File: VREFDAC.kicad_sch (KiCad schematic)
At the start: 11 parts, among them U34 AD7841, U44 AD586, U45 AD586

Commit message: Add component values, some more nets
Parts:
- C160, C161, C162, C163, C164, C165: value ? -> 0.047uF
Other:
- moved on the sheet: C162, C163, C165
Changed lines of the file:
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@@
 	)
 	(junction
-		(at 199.39 48.26)
+		(at 195.58 48.26)
 		(diameter 0)
 		(color 0 0 0 0)
@@
 	)
 	(junction
-		(at 162.56 46.99)
+		(at 166.37 46.99)
 		(diameter 0)
 		(color 0 0 0 0)
@@
 	(wire
 		(pts
-			(xy 162.56 46.99) (xy 162.56 50.8)
+			(xy 166.37 46.99) (xy 166.37 50.8)
 		)
 		(stroke
@@
 	(wire
 		(pts
-			(xy 199.39 48.26) (xy 199.39 50.8)
+			(xy 195.58 48.26) (xy 195.58 50.8)
 		)
 		(stroke
@@
 	(wire
 		(pts
-			(xy 199.39 48.26) (xy 186.69 48.26)
-		)
-		(stroke
-			(width 0)
-			(type default)
-		)
-	)
-	(wire
-		(pts
-			(xy 215.9 31.75) (xy 209.55 31.75)
+			(xy 227.33 31.75) (xy 215.9 31.75)
 		)
 		(stroke
@@
 	(wire
 		(pts
+			(xy 195.58 48.26) (xy 205.74 48.26)
+		)
+		(stroke
+			(width 0)
+			(type default)
+		)
+	)
+	(wire
+		(pts
 			(xy 165.1 121.92) (xy 165.1 148.59)
 		)
@@
 	(wire
 		(pts
-			(xy 162.56 45.72) (xy 162.56 46.99)
+			(xy 166.37 45.72) (xy 166.37 46.99)
 		)
 		(stroke
@@
 	(wire
 		(pts
-			(xy 205.74 48.26) (xy 199.39 48.26)
-		)
-		(stroke
-			(width 0)
-			(type default)
-		)
-	)
-	(wire
-		(pts
 			(xy 215.9 26.67) (xy 215.9 31.75)
 		)
@@
 	(wire
 		(pts
-			(xy 209.55 31.75) (xy 209.55 33.02)
+			(xy 227.33 31.75) (xy 227.33 33.02)
 		)
 		(stroke
@@
 	(wire
 		(pts
+			(xy 195.58 48.26) (xy 186.69 48.26)
+		)
+		(stroke
+			(width 0)
+			(type default)
+		)
+	)
+	(wire
+		(pts
 			(xy 93.98 99.06) (xy 124.46 99.06)
 		)
@@
 	(wire
 		(pts
-			(xy 152.4 46.99) (xy 162.56 46.99)
+			(xy 152.4 46.99) (xy 166.37 46.99)
 		)
 		(stroke
@@
 	(symbol
 		(lib_id "power:GND")
-		(at 209.55 38.1 0)
+		(at 227.33 38.1 0)
 		(mirror y)
 		(unit 1)
@@
 		(fields_autoplaced yes)
 		(property "Reference" "#PWR0229"
-			(at 209.55 44.45 0)
+			(at 227.33 44.45 0)
 			(effects
 				(font
@@
 		)
 		(property "Value" "GND"
-			(at 209.55 43.18 0)
+			(at 227.33 43.18 0)
 			(effects
 				(font
@@
 		)
 		(property "Footprint" ""
-			(at 209.55 38.1 0)
+			(at 227.33 38.1 0)
 			(effects
 				(font
@@
 		)
 		(property "Datasheet" ""
-			(at 209.55 38.1 0)
+			(at 227.33 38.1 0)
 			(effects
 				(font
@@
 		)
 		(property "Description" "Power symbol creates a global label with name \"GND\" , ground"
-			(at 209.55 38.1 0)
+			(at 227.33 38.1 0)
 			(effects
 				(font
@@
 			)
 		)
-		(property "Value" "?"
+		(property "Value" "0.047uF"
 			(at 154.94 54.6162 0)
 			(effects
@@
 			)
 		)
-		(property "Value" "?"
+		(property "Value" "0.047uF"
 			(at 148.59 146.0562 0)
 			(effects
@@
 	(symbol
 		(lib_id "power:+12V")
-		(at 162.56 45.72 0)
+		(at 166.37 45.72 0)
 		(unit 1)
 		(exclude_from_sim no)
@@
 		(dnp no)
 		(property "Reference" "#PWR0231"
-			(at 162.56 49.53 0)
+			(at 166.37 49.53 0)
 			(effects
 				(font
@@
 		)
 		(property "Value" "+12V"
-			(at 162.56 40.64 0)
+			(at 166.37 40.64 0)
 			(effects
 				(font
@@
 		)
 		(property "Footprint" ""
-			(at 162.56 45.72 0)
+			(at 166.37 45.72 0)
 			(effects
 				(font
@@
 		)
 		(property "Datasheet" ""
-			(at 162.56 45.72 0)
+			(at 166.37 45.72 0)
 			(effects
 				(font
@@
 		)
 		(property "Description" "Power symbol creates a global label with name \"+12V\""
-			(at 162.56 45.72 0)
+			(at 166.37 45.72 0)
 			(effects
 				(font
@@
 	(symbol
 		(lib_id "power:GND")
-		(at 162.56 55.88 0)
+		(at 166.37 55.88 0)
 		(unit 1)
 		(exclude_from_sim no)
@@
 		(fields_autoplaced yes)
 		(property "Reference" "#PWR0226"
-			(at 162.56 62.23 0)
+			(at 166.37 62.23 0)
 			(effects
 				(font
@@
 		)
 		(property "Value" "GND"
-			(at 162.56 60.96 0)
+			(at 166.37 60.96 0)
 			(effects
 				(font
@@
 		)
 		(property "Footprint" ""
-			(at 162.56 55.88 0)
+			(at 166.37 55.88 0)
 			(effects
 				(font
@@
 		)
 		(property "Datasheet" ""
-			(at 162.56 55.88 0)
+			(at 166.37 55.88 0)
 			(effects
 				(font
@@
 		)
 		(property "Description" "Power symbol creates a global label with name \"GND\" , ground"
-			(at 162.56 55.88 0)
+			(at 166.37 55.88 0)
 			(effects
 				(font
@@
 			)
 		)
-		(property "Value" "?"
+		(property "Value" "0.047uF"
 			(at 218.44 154.9462 0)
 			(effects
@@
 	(symbol
 		(lib_id "Device:C_Small")
-		(at 199.39 53.34 0)
+		(at 195.58 53.34 0)
 		(unit 1)
 		(exclude_from_sim no)
@@
 		(fields_autoplaced yes)
 		(property "Reference" "C163"
-			(at 201.93 52.0762 0)
+			(at 198.12 52.0762 0)
 			(effects
 				(font
@@
 			)
 		)
-		(property "Value" "?"
-			(at 201.93 54.6162 0)
+		(property "Value" "0.047uF"
+			(at 198.12 54.6162 0)
 			(effects
 				(font
@@
 		)
 		(property "Footprint" "hp16717:HP_0805"
-			(at 199.39 53.34 0)
+			(at 195.58 53.34 0)
 			(effects
 				(font
@@
 		)
 		(property "Datasheet" "~"
-			(at 199.39 53.34 0)
+			(at 195.58 53.34 0)
 			(effects
 				(font
@@
 		)
 		(property "Description" "Unpolarized capacitor, small symbol"
-			(at 199.39 53.34 0)
+			(at 195.58 53.34 0)
 			(effects
 				(font
@@
 	(symbol
 		(lib_id "Device:C_Small")
-		(at 162.56 53.34 0)
+		(at 166.37 53.34 0)
 		(unit 1)
 		(exclude_from_sim no)
@@
 		(fields_autoplaced yes)
 		(property "Reference" "C162"
-			(at 165.1 52.0762 0)
+			(at 168.91 52.0762 0)
 			(effects
 				(font
@@
 			)
 		)
-		(property "Value" "?"
-			(at 165.1 54.6162 0)
+		(property "Value" "0.047uF"
+			(at 168.91 54.6162 0)
 			(effects
 				(font
@@
 		)
 		(property "Footprint" "hp16717:HP_0805"
-			(at 162.56 53.34 0)
+			(at 166.37 53.34 0)
 			(effects
 				(font
@@
 		)
 		(property "Datasheet" "~"
-			(at 162.56 53.34 0)
+			(at 166.37 53.34 0)
 			(effects
 				(font
@@
 		)
 		(property "Description" "Unpolarized capacitor, small symbol"
-			(at 162.56 53.34 0)
+			(at 166.37 53.34 0)
 			(effects
 				(font
@@
 	(symbol
 		(lib_id "Device:C_Small")
-		(at 209.55 35.56 0)
+		(at 227.33 35.56 0)
 		(mirror y)
 		(unit 1)
@@
 		(fields_autoplaced yes)
 		(property "Reference" "C165"
-			(at 207.01 34.2962 0)
+			(at 229.87 34.2962 0)
 			(effects
 				(font
 					(size 1.27 1.27)
 				)
-				(justify left)
+				(justify right)
 			)
 		)
-		(property "Value" "?"
-			(at 207.01 36.8362 0)
+		(property "Value" "0.047uF"
+			(at 229.87 36.8362 0)
 			(effects
 				(font
 					(size 1.27 1.27)
 				)
-				(justify left)
+				(justify right)
 			)
 		)
 		(property "Footprint" "hp16717:HP_0805"
-			(at 209.55 35.56 0)
+			(at 227.33 35.56 0)
 			(effects
 				(font
@@
 		)
 		(property "Datasheet" "~"
-			(at 209.55 35.56 0)
+			(at 227.33 35.56 0)
 			(effects
 				(font
@@
 		)
 		(property "Description" "Unpolarized capacitor, small symbol"
-			(at 209.55 35.56 0)
+			(at 227.33 35.56 0)
 			(effects
 				(font
@@
 	(symbol
 		(lib_id "power:GND")
-		(at 199.39 55.88 0)
+		(at 195.58 55.88 0)
 		(unit 1)
 		(exclude_from_sim no)
@@
 		(fields_autoplaced yes)
 		(property "Reference" "#PWR0227"
-			(at 199.39 62.23 0)
+			(at 195.58 62.23 0)
 			(effects
 				(font
@@
 		)
 		(property "Value" "GND"
-			(at 199.39 60.96 0)
+			(at 195.58 60.96 0)
 			(effects
 				(font
@@
 		)
 		(property "Footprint" ""
-			(at 199.39 55.88 0)
+			(at 195.58 55.88 0)
 			(effects
 				(font
@@
 		)
 		(property "Datasheet" ""
-			(at 199.39 55.88 0)
+			(at 195.58 55.88 0)
 			(effects
 				(font
@@
 		)
 		(property "Description" "Power symbol creates a global label with name \"GND\" , ground"
-			(at 199.39 55.88 0)
+			(at 195.58 55.88 0)
 			(effects
 				(font

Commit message: complete outer layers
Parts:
- U34: footprint Package_QFP:Microchip_PQFP-44_10x10mm_P0.8mm -> hp16717:HP_LQFP-44_10x10mm_P0.8mm
- U44, U45: footprint Package_SO:SOIC-8_3.9x4.9mm_P1.27mm -> hp16717:HP_SO-8_3.9x4.9mm_P1.27mm
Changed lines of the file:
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@@
 			)
 		)
-		(property "Footprint" "Package_SO:SOIC-8_3.9x4.9mm_P1.27mm"
+		(property "Footprint" "hp16717:HP_SO-8_3.9x4.9mm_P1.27mm"
 			(at 217.17 46.99 0)
 			(effects
@@
 			)
 		)
-		(property "Footprint" "Package_QFP:Microchip_PQFP-44_10x10mm_P0.8mm"
+		(property "Footprint" "hp16717:HP_LQFP-44_10x10mm_P0.8mm"
 			(at 127 60.96 0)
 			(effects
@@
 			)
 		)
-		(property "Footprint" "Package_SO:SOIC-8_3.9x4.9mm_P1.27mm"
+		(property "Footprint" "hp16717:HP_SO-8_3.9x4.9mm_P1.27mm"
 			(at 214.63 132.08 0)
 			(effects

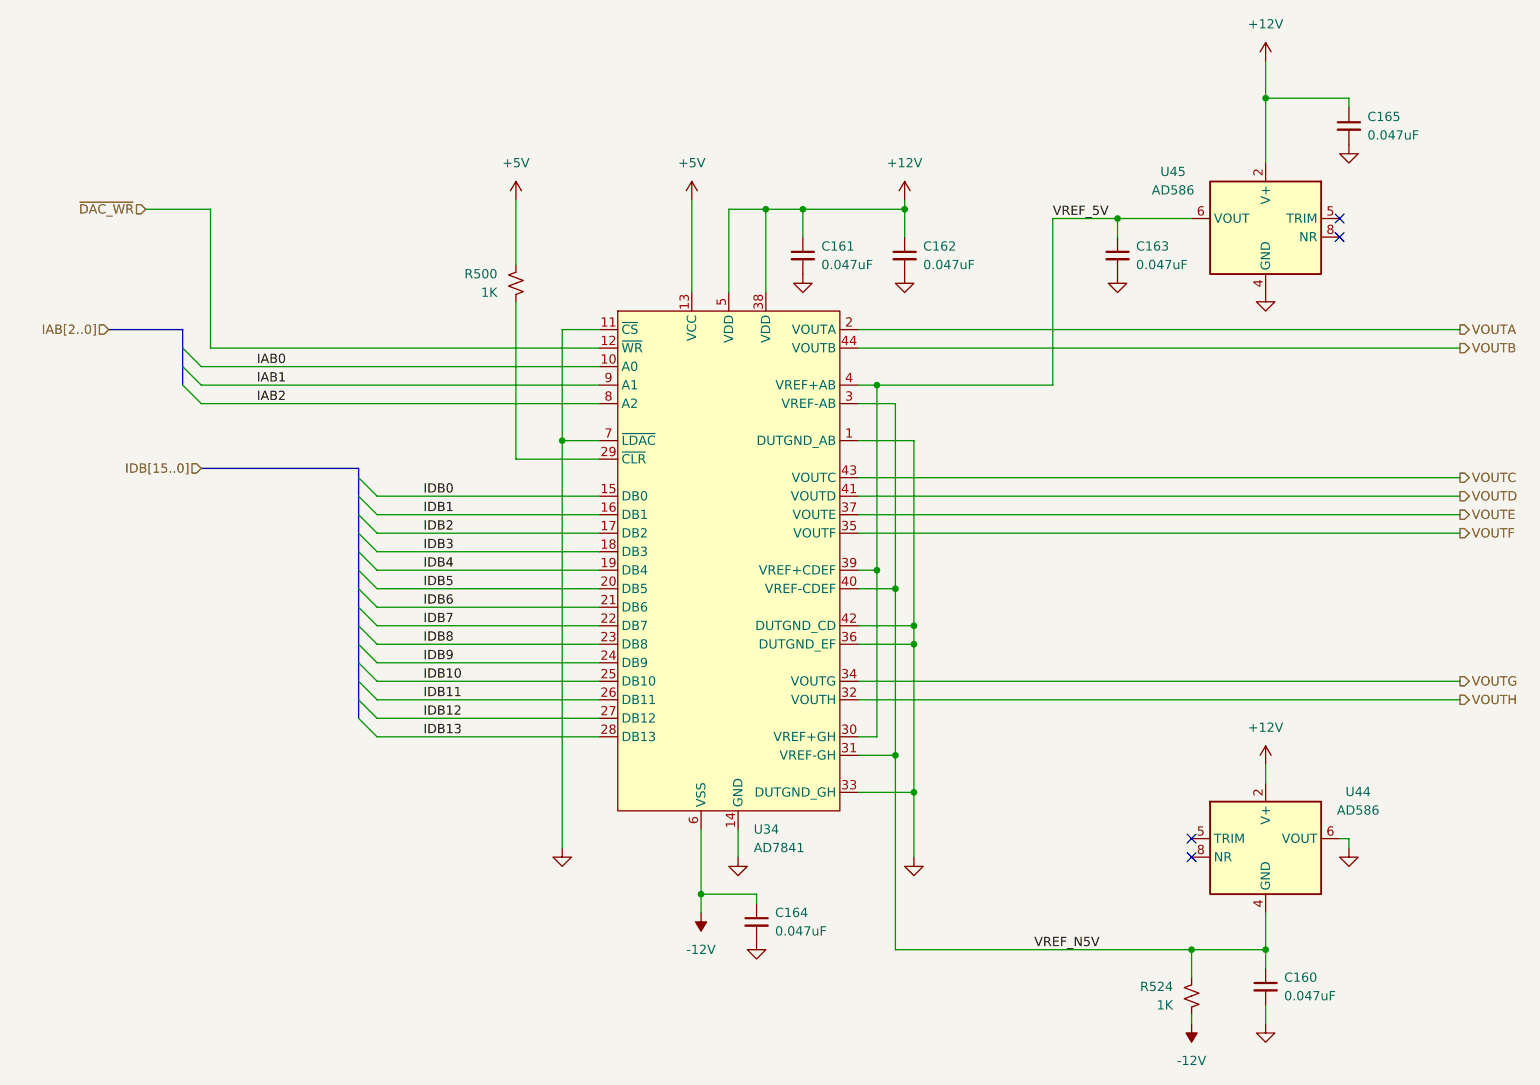
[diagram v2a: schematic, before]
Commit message: add test points
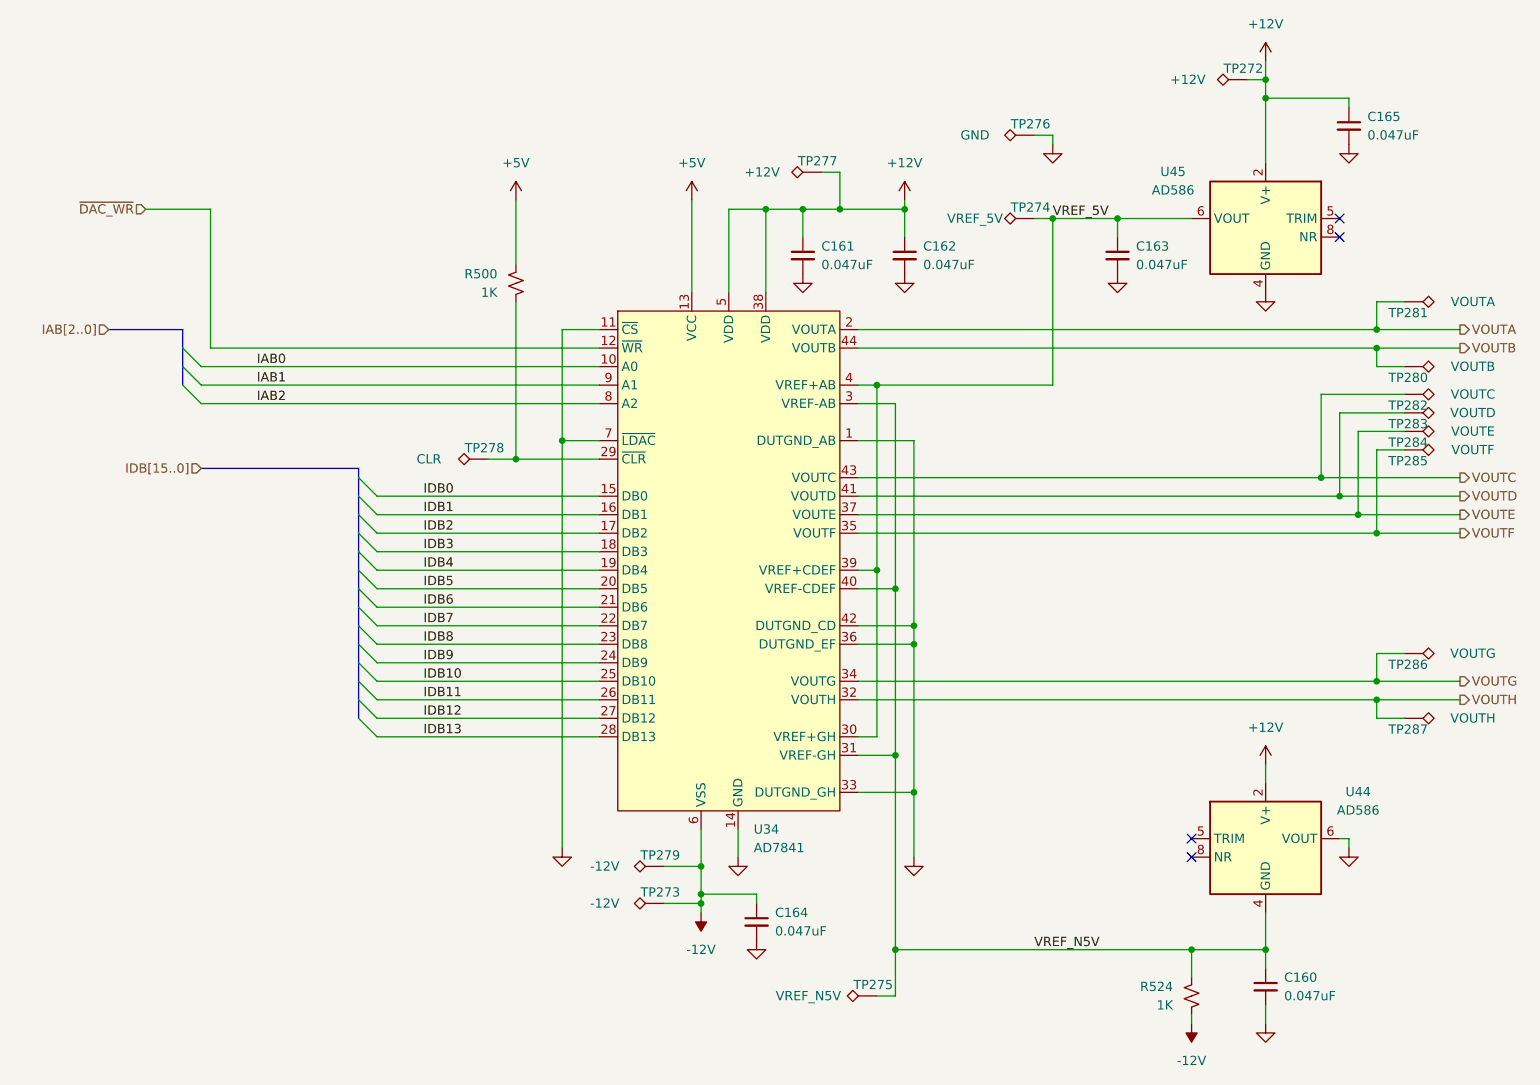
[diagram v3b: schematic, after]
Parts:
- added TP272, TP277: +12V, hp16717:HP_TP30, symbol Connector:TestPoint_Alt
- added TP273, TP279: -12V, hp16717:HP_TP30, symbol Connector:TestPoint_Alt
- added TP274: VREF_5V, hp16717:HP_TP30, symbol Connector:TestPoint_Alt
- added TP275: VREF_N5V, hp16717:HP_TP30, symbol Connector:TestPoint_Alt
- added TP276: GND, hp16717:HP_TP30, symbol Connector:TestPoint_Alt
- added TP278: CLR, hp16717:HP_TP30, symbol Connector:TestPoint_Alt
- added TP280: VOUTB, hp16717:HP_TP30, symbol Connector:TestPoint_Alt
- added TP281: VOUTA, hp16717:HP_TP30, symbol Connector:TestPoint_Alt
- added TP282: VOUTC, hp16717:HP_TP30, symbol Connector:TestPoint_Alt
- added TP283: VOUTD, hp16717:HP_TP30, symbol Connector:TestPoint_Alt
- added TP284: VOUTE, hp16717:HP_TP30, symbol Connector:TestPoint_Alt
- added TP285: VOUTF, hp16717:HP_TP30, symbol Connector:TestPoint_Alt
- added TP286: VOUTG, hp16717:HP_TP30, symbol Connector:TestPoint_Alt
- added TP287: VOUTH, hp16717:HP_TP30, symbol Connector:TestPoint_Alt
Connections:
- net +12V: now also TP272.1, TP277.1
- net -12V: now also TP273.1, TP279.1
- net GND: now also TP276.1
- net VOUTA: now also TP281.1
- net VOUTB: now also TP280.1
- net VOUTC: now also TP282.1
- net VOUTD: now also TP283.1
- net VOUTE: now also TP284.1
- net VOUTF: now also TP285.1
- net VOUTG: now also TP286.1
- net VOUTH: now also TP287.1
- net VREF_5V: now also TP274.1
- net VREF_N5V: now also TP275.1
- net at R500.1, U34.29 (~{CLR}): now also TP278.1
